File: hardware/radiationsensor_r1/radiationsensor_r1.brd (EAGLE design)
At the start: 40 x 62.5 mm, 37 parts, among them CN1 1X06, U1 LMP7721, U2 MAX4477, U4 MAX4477, U5 50k

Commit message: minor changes
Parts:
- moved U5 1.41 mm to (39.6, 29.5)
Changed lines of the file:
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@@
 <attribute name="VALUE" x="38.637" y="43.4244" size="0.6096" layer="21" rot="R90"/>
 </element>
-<element name="U5" library="openct" package="SOT-23-8" value="50k" x="38.625" y="30.5" rot="R270"/>
+<element name="U5" library="openct" package="SOT-23-8" value="50k" x="39.625" y="29.5" rot="R270"/>
 <element name="C10" library="openct" package="0603" value="0.1uF" x="38.5" y="46" smashed="yes" rot="R180">
 <attribute name="NAME" x="37.0494" y="46.8496" size="0.6096" layer="21"/>
@@
 <wire x1="59.5" y1="36.35" x2="56.54" y2="35.905" width="0" layer="19" extent="1-1"/>
 <wire x1="61.5" y1="32.6" x2="59.5" y2="36.35" width="0" layer="19" extent="1-1"/>
-<wire x1="37.325" y1="30.175" x2="37.375" y2="39.85" width="0" layer="19" extent="1-1"/>
-<wire x1="44.5508" y1="19.5738" x2="37.325" y2="30.175" width="0" layer="19" extent="1-1"/>
+<wire x1="38.325" y1="29.175" x2="37.375" y2="39.85" width="0" layer="19" extent="1-1"/>
+<wire x1="44.5508" y1="19.5738" x2="38.325" y2="29.175" width="0" layer="19" extent="1-1"/>
 <wire x1="44.5" y1="17.5" x2="44.5508" y2="19.5738" width="0" layer="19" extent="1-1"/>
 <wire x1="64.75" y1="19.9" x2="61.5" y2="32.6" width="0" layer="19" extent="1-1"/>
@@
 <wire x1="39.625" y1="38.15" x2="50.46" y2="34.635" width="0" layer="19" extent="1-1"/>
 <wire x1="37.375" y1="38.15" x2="39" y2="36.025" width="0" layer="19" extent="1-1"/>
-<wire x1="37.325" y1="31.475" x2="37.375" y2="38.15" width="0" layer="19" extent="1-1"/>
+<wire x1="38.325" y1="30.475" x2="37.375" y2="38.15" width="0" layer="19" extent="1-1"/>
 </signal>
 <signal name="N$17">
 <contactref element="U5" pad="8"/>
 <contactref element="R15" pad="1"/>
-<wire x1="39.925" y1="31.475" x2="39.625" y2="33.65" width="0" layer="19" extent="1-1"/>
+<wire x1="40.925" y1="30.475" x2="39.625" y2="33.65" width="0" layer="19" extent="1-1"/>
 </signal>
 <signal name="MOSI">
@@
 <signal name="SCLK">
 <contactref element="U5" pad="4"/>
-<wire x1="37.325" y1="29.525" x2="37.325" y2="28.55" width="0.254" layer="1"/>
-<wire x1="37.325" y1="28.55" x2="38.125" y2="27.75" width="0" layer="19" extent="1-16"/>
-<wire x1="38.125" y1="27.75" x2="17.75" y2="25" width="0" layer="19" extent="1-16"/>
+<wire x1="38.325" y1="28.525" x2="38.325" y2="27.55" width="0.254" layer="1"/>
+<wire x1="38.325" y1="27.55" x2="39.125" y2="26.75" width="0" layer="19" extent="1-16"/>
+<wire x1="39.125" y1="26.75" x2="17.75" y2="25" width="0" layer="19" extent="1-16"/>
 <wire x1="17.75" y1="25" x2="17.75" y2="25" width="0" layer="19" extent="1-16"/>
-<wire x1="17.75" y1="25" x2="37.25" y2="29" width="0" layer="19" extent="1-16"/>
-<wire x1="37.25" y1="29" x2="37.25" y2="29" width="0" layer="19" extent="1-16"/>
-<wire x1="37.25" y1="29" x2="49.25" y2="24.25" width="0" layer="19" extent="1-16"/>
+<wire x1="17.75" y1="25" x2="38.25" y2="28" width="0" layer="19" extent="1-16"/>
+<wire x1="38.25" y1="28" x2="38.25" y2="28" width="0" layer="19" extent="1-16"/>
+<wire x1="38.25" y1="28" x2="49.25" y2="24.25" width="0" layer="19" extent="1-16"/>
 <wire x1="49.25" y1="24.25" x2="50.325" y2="23.175" width="0" layer="19" extent="1-16"/>
 </signal>
@@
 <contactref element="U5" pad="2"/>
 <contactref element="C17" pad="1"/>
-<wire x1="37.325" y1="30.825" x2="38.05" y2="30.825" width="0.254" layer="1"/>
-<wire x1="38.05" y1="30.825" x2="38.625" y2="30.25" width="0.254" layer="1" curve="-90"/>
-<wire x1="38.625" y1="30.25" x2="38.625" y2="29.25" width="0.254" layer="1"/>
+<wire x1="38.325" y1="29.825" x2="39.05" y2="29.825" width="0.254" layer="1"/>
+<wire x1="39.05" y1="29.825" x2="39.625" y2="29.25" width="0.254" layer="1" curve="-90"/>
+<wire x1="39.625" y1="29.25" x2="39.625" y2="28.25" width="0.254" layer="1"/>
 <wire x1="44.5508" y1="21.2738" x2="44.56185" y2="21.26275" width="0.3048" layer="1"/>
-<wire x1="44.5508" y1="21.2738" x2="38.625" y2="29.25" width="0" layer="19" extent="1-1"/>
+<wire x1="44.5508" y1="21.2738" x2="39.625" y2="28.25" width="0" layer="19" extent="1-1"/>
 <wire x1="47.25" y1="7.127" x2="44.5508" y2="21.2738" width="0" layer="19" extent="1-1"/>
 </signal>

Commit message: radiation sensor r1 layout nearly complete
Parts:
- removed C17: 0.1uF, openct:0603
- added C16: 1uF, openct:0603
- added R16: THERM, openct:0603
- added R17: 10k, openct:0603
- C14: value 10uF 16V -> 10uF 10V
- C15: value 0.1uF -> 0.1uF 50V
- C4: value 1uF -> 1uF 50V
- CN1: value 1X06 -> 1X09; device openct:1X06 -> openct:1X09
- moved C14 20.5 mm to (62.8, 39.4)
- moved CN1 16.4 mm to (51.0, 23.0)
- moved R15 5.86 mm to (42.9, 29.6)
- moved R14 4.51 mm to (41.9, 38.8)
- moved C13 4.38 mm to (44.0, 38.8)
- moved R9 3.99 mm to (40.4, 45.5), turned to 90 degrees
- moved R8 3.89 mm to (42.5, 45.5), turned to 270 degrees
- moved U5 2.64 mm to (39.4, 32.1), turned to 180 degrees
- moved R4 2.34 mm to (61.1, 47.2), turned to 270 degrees
- moved C6 1.27 mm to (49.4, 39.8)
- moved C11 1.25 mm to (61.5, 34.2)
- moved C12 1.25 mm to (61.5, 30.5)
- moved C7 1.25 mm to (61.1, 43.2)
- moved C8 1.25 mm to (58.1, 39.8)
- moved C9 1.25 mm to (45.9, 44.5)
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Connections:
- removed net N$15: C14.1
- removed net VLOGIC: C17.1, CN1.1, U5.2
- new net VTEMP: CN1.1, R16.2, R17.1
- net 5V: now also C14.1, C16.1, CN1.8, R17.2, U5.2; no longer CN1.5
- net COMP_OUT: now also CN1.6; no longer CN1.3
- net CS: now also CN1.2
- net GND: now also C16.2, CN1.7, R16.1; no longer C17.2, CN1.4
- net MOSI: now also CN1.4
- net SCLK: now also CN1.3
- net VBIAS: now also CN1.9; no longer CN1.6
- net VOUT: now also CN1.5; no longer CN1.2
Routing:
- net 5V: track 20.5 -> 110.8 mm, vias 1 -> 6
- net VBIAS: track 2.25 -> 55.0 mm, vias 0 -> 1
- net VTEMP: track 0.00 -> 20.3 mm
- net V_COMP: track 2.17 -> 21.1 mm, vias 1 -> 2
- net N$11: track 4.72 -> 23.3 mm
- net SCLK: track 0.97 -> 17.5 mm
- net MOSI: track 0.00 -> 15.9 mm
- net COMP_OUT: track 3.29 -> 17.9 mm
- net V/2: track 13.1 -> 24.5 mm, vias 4 -> 5
- net VOUT: track 22.8 -> 34.1 mm
- net CS: track 0.00 -> 9.75 mm, vias 0 -> 1
- net N$2: track 3.51 -> 12.6 mm
- net N$17: track 0.00 -> 4.23 mm
- net N$7: track 9.99 -> 13.0 mm
- net VLOGIC: track 2.55 -> 0.00 mm
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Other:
- board size 40 x 62.5 mm -> 30 x 46.5 mm
- board text removed: "ICD3"
- board text removed: "PIC24FV32KA301"

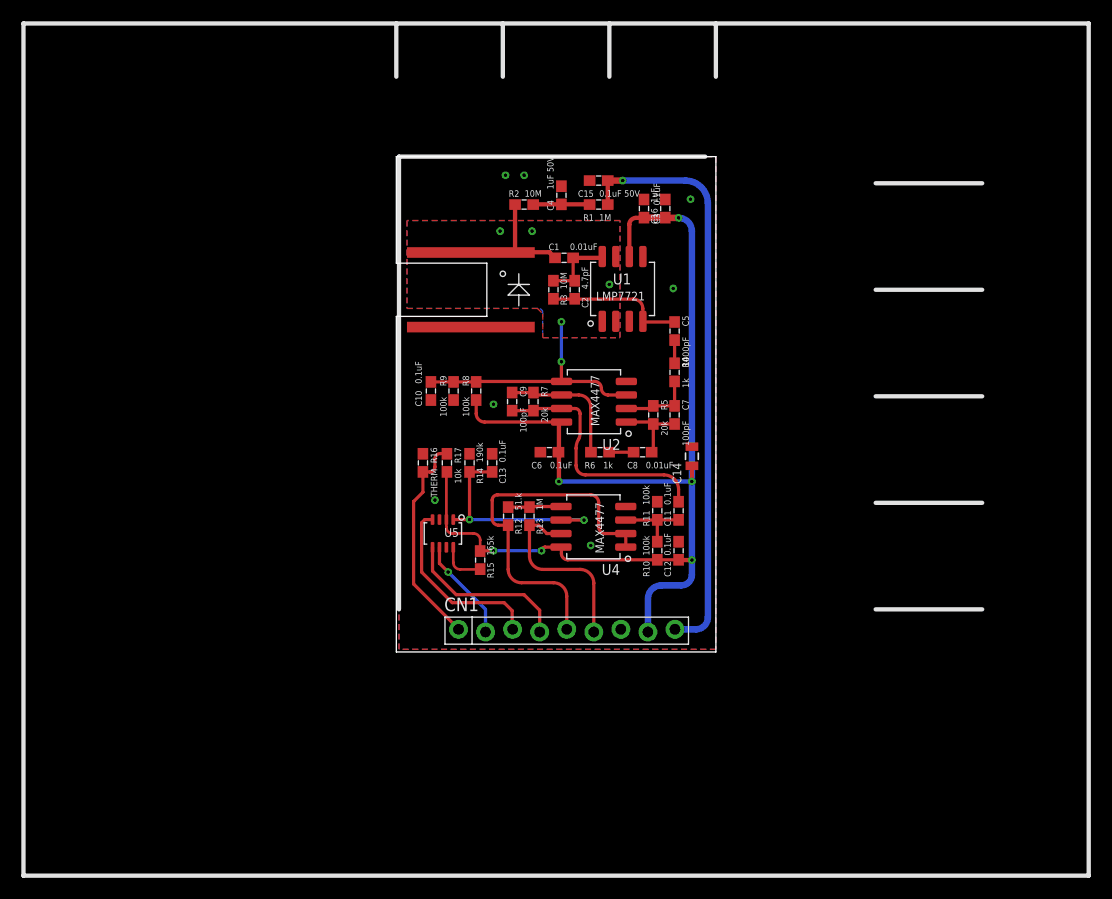
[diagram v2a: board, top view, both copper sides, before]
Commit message: schematic and board cleanup
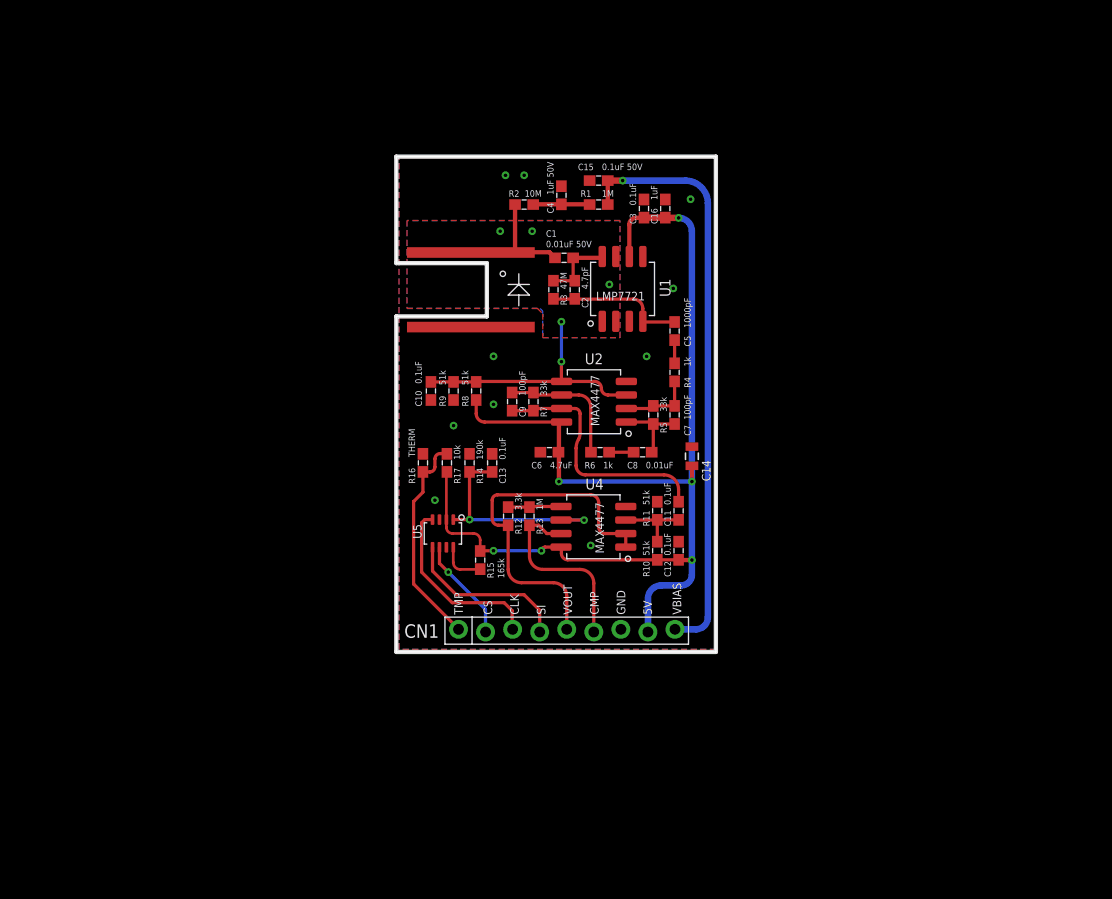
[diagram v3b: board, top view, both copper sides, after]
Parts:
- C1: value 0.01uF -> 0.01uF 50V
- C6: value 0.1uF -> 4.7uF
- R10, R11, R8, R9: value 100k -> 51k
- R12: value 51.k -> 3.3k
- R3: value 10M -> 47M
- R5, R7: value 20k -> 33k
- renumbered D2 to D1
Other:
- board text added: "CLK"
- board text added: "CMP"
- board text added: "CS"
- board text added: "SI"
- board text added: "TMP"
- board text added: "VOUT"
- board text added: "high energy particle detector rev1"
- board text added: "peter jansen june/2015"
- board text removed: "SCL"
- board text removed: "SDA"
- board text removed: "VLOGIC"
- board text removed: "detector rev0"
- board text removed: "high energy particle"
- board text removed: "peter jansen apr/2015"

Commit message: Added part in library for radiation sensor rev1
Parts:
- R16: value THERM -> NCP18XV103
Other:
- board text added: "THERM"
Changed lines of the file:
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@@
 <setting verticaltext="up"/>
 </settings>
-<grid distance="0.125" unitdist="mm" unit="mm" style="lines" multiple="1" display="yes" altdistance="0.025" altunitdist="inch" altunit="inch"/>
+<grid distance="0.25" unitdist="mm" unit="mm" style="lines" multiple="1" display="yes" altdistance="0.025" altunitdist="inch" altunit="inch"/>
 <layers>
 <layer number="1" name="Top" color="4" fill="1" visible="yes" active="yes"/>
@@
 <text x="64" y="26.25" size="0.8128" layer="22" rot="MR0">high energy particle detector rev1</text>
 <text x="64" y="25" size="0.8128" layer="22" rot="MR0">peter jansen june/2015</text>
+<text x="36.75" y="39" size="0.6096" layer="21" rot="R90">THERM</text>
 </plain>
 <attributes>
@@
 </element>
 <element name="D1" library="openct" package="BPW34S-4STACK-SIDEMOUNT" value="BPW34S" x="46" y="55" rot="R90"/>
-<element name="R16" library="openct" package="0603" value="THERM" x="37.5" y="38.75" smashed="yes" rot="R270">
+<element name="R16" library="openct" package="0603" value="NCP18XV103" x="37.5" y="38.75" smashed="yes" rot="R270">
 <attribute name="NAME" x="36.7754" y="36.7994" size="0.6096" layer="21" rot="R90"/>
-<attribute name="VALUE" x="36.762" y="39.2994" size="0.6096" layer="21" rot="R90"/>
 </element>
 <element name="R17" library="openct" package="0603" value="10k" x="39.75" y="38.75" smashed="yes" rot="R270">
@@
 <via x="44.125" y="48.75" extent="1-16" drill="0.3302"/>
 <via x="40.375" y="42.25" extent="1-16" drill="0.3302"/>
+<via x="56.5" y="36" extent="1-16" drill="0.3302"/>
 </signal>
 <signal name="5V">
